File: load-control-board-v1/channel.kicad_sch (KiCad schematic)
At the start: 34 parts, among them Q1 AO3400A, Q2 AO3400A, Q3 IRFP7530PBF, U10 OPA188xxDBV, U11 OPA188xxDBV, U12 INA186A1IDCKR

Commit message: Move to layout stage
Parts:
- TP0a1, TP0c1, TP2, TP3: footprint TestPoint:TestPoint_Keystone_5019_Miniature -> TestPoint:TestPoint_Keystone_5015_Micro_Mini
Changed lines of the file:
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@@
 			)
 		)
-		(property "Footprint" "TestPoint:TestPoint_Keystone_5019_Miniature"
+		(property "Footprint" "TestPoint:TestPoint_Keystone_5015_Micro_Mini"
 			(at 190.5 38.1 0)
 			(effects
@@
 			)
 		)
-		(property "Footprint" "TestPoint:TestPoint_Keystone_5019_Miniature"
+		(property "Footprint" "TestPoint:TestPoint_Keystone_5015_Micro_Mini"
 			(at 77.47 60.96 0)
 			(effects
@@
 			)
 		)
-		(property "Footprint" "TestPoint:TestPoint_Keystone_5019_Miniature"
+		(property "Footprint" "TestPoint:TestPoint_Keystone_5015_Micro_Mini"
 			(at 115.57 43.18 0)
 			(effects
@@
 			)
 		)
-		(property "Footprint" "TestPoint:TestPoint_Keystone_5019_Miniature"
+		(property "Footprint" "TestPoint:TestPoint_Keystone_5015_Micro_Mini"
 			(at 204.47 133.35 0)
 			(effects

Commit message: initial layout
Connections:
- net at R21.1, R22.2, R23.2: no longer C15.1, R20.1
- net at R21.2, TP2.1, U10.1: now also C15.1, R20.1
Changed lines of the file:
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@@
+	)
+	(junction
+		(at 86.36 72.39)
+		(diameter 0)
+		(color 0 0 0 0)
 	)
 	(junction
@@
 	)
 	(junction
-		(at 86.36 72.39)
-		(diameter 0)
-		(color 0 0 0 0)
-	)
-	(junction
 		(at 91.44 60.96)
 		(diameter 0)
@@
 		(color 0 0 0 0)
 	)
-	(junction
-		(at 86.36 60.96)
-		(diameter 0)
-		(color 0 0 0 0)
-	)
 	(wire
 		(pts
@@
 	(wire
 		(pts
+			(xy 86.36 67.31) (xy 72.39 67.31)
+		)
+		(stroke
+			(width 0)
+			(type default)
+		)
+	)
+	(wire
+		(pts
+			(xy 72.39 67.31) (xy 72.39 60.96)
+		)
+		(stroke
+			(width 0)
+			(type default)
+		)
+	)
+	(wire
+		(pts
 			(xy 185.42 45.72) (xy 200.66 45.72)
 		)
@@
 	(wire
 		(pts
-			(xy 86.36 60.96) (xy 91.44 60.96)
+			(xy 81.28 60.96) (xy 91.44 60.96)
 		)
 		(stroke
@@
 	(wire
 		(pts
-			(xy 81.28 60.96) (xy 86.36 60.96)
-		)
-		(stroke
-			(width 0)
-			(type default)
-		)
-	)
-	(wire
-		(pts
 			(xy 106.68 60.96) (xy 106.68 69.85)
 		)
@@
 	(wire
 		(pts
+			(xy 86.36 72.39) (xy 86.36 67.31)
+		)
+		(stroke
+			(width 0)
+			(type default)
+		)
+	)
+	(wire
+		(pts
 			(xy 182.88 45.72) (xy 185.42 45.72)
 		)
@@
 		)
 		(stroke
-			(width 0)
-			(type default)
-		)
-	)
-	(wire
-		(pts
-			(xy 86.36 60.96) (xy 86.36 72.39)
-		)
-		(stroke

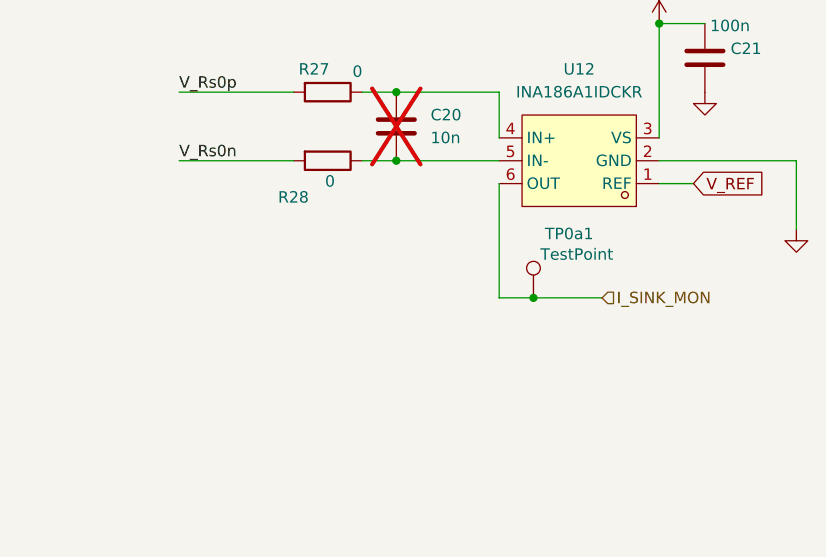
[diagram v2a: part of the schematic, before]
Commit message: Define the connector pinout to control board, import current connector
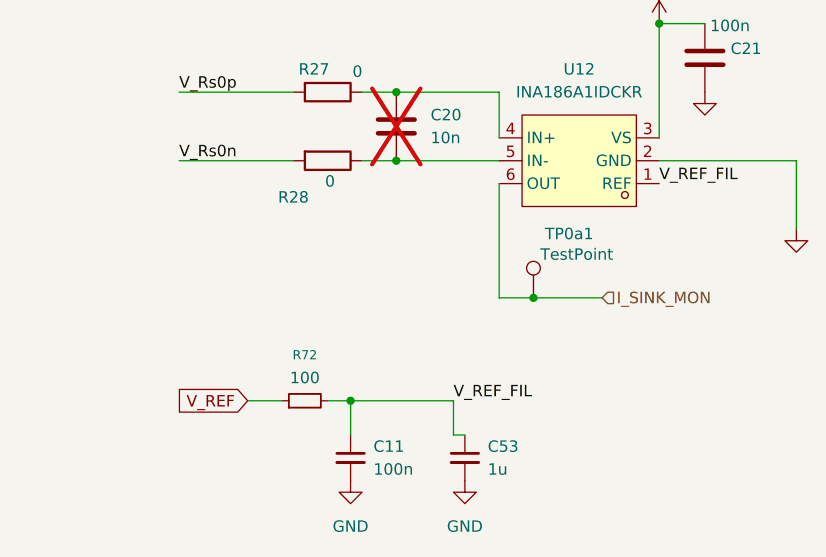
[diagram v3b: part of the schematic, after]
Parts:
- added C11: 100n, symbol Device:C_Small
- added C53: 1u, symbol Device:C_Small
- added R72: 100, symbol Device:R_Small
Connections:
- net GND: now also C11.2, C53.2
- net V_REF: now also R72.1; no longer U12.1 (REF)
- new net V_REF_FIL: C11.1, C53.1, R72.2, U12.1 (REF)

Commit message: layout before check
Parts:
- C11: footprint (none) -> Capacitor_SMD:C_0603_1608Metric
- C53, R72: footprint (none) -> Resistor_SMD:R_0603_1608Metric
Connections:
- net 5V renamed +5V
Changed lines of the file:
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@@
 			)
 		)
-		(property "Value" "5V"
+		(property "Value" "+5V"
 			(at 213.614 98.806 0)
 			(effects
@@
 			)
 		)
-		(property "Footprint" ""
+		(property "Footprint" "Capacitor_SMD:C_0603_1608Metric"
 			(at 179.07 151.13 0)
 			(effects
@@
 			)
 		)
-		(property "Footprint" ""
+		(property "Footprint" "Resistor_SMD:R_0603_1608Metric"
 			(at 191.77 151.13 0)
 			(effects
@@
 			)
 		)
-		(property "Footprint" ""
+		(property "Footprint" "Resistor_SMD:R_0603_1608Metric"
 			(at 173.99 144.78 0)
 			(effects

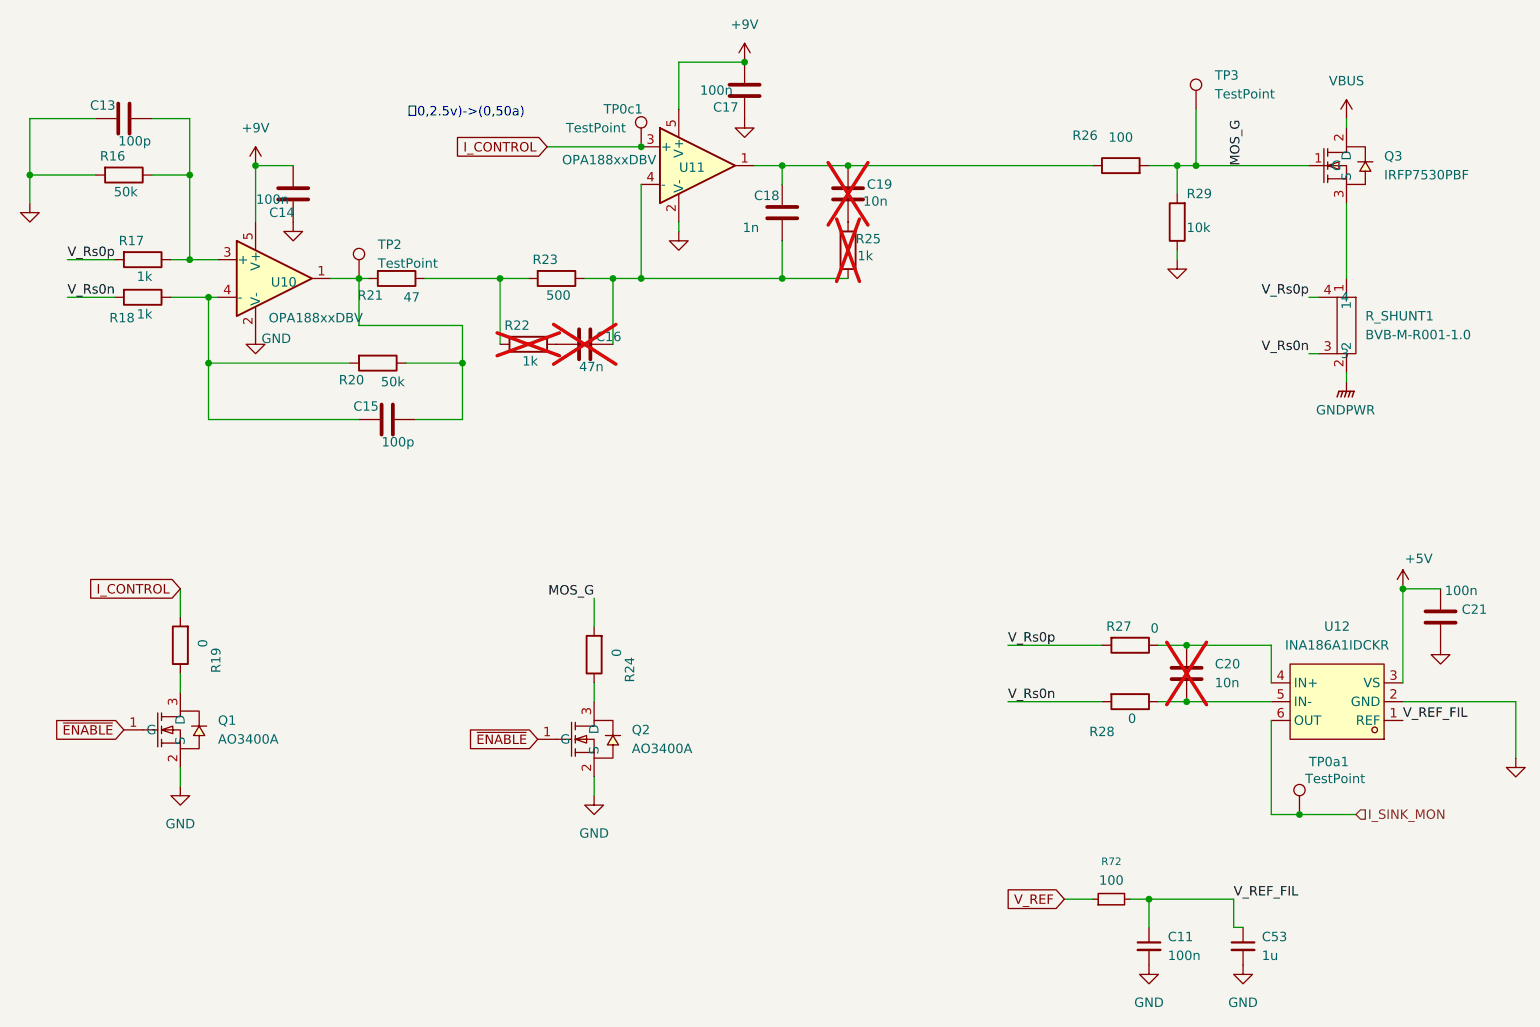
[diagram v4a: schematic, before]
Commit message: Add filled zone for mosfet, change terminal to from THO to SMT
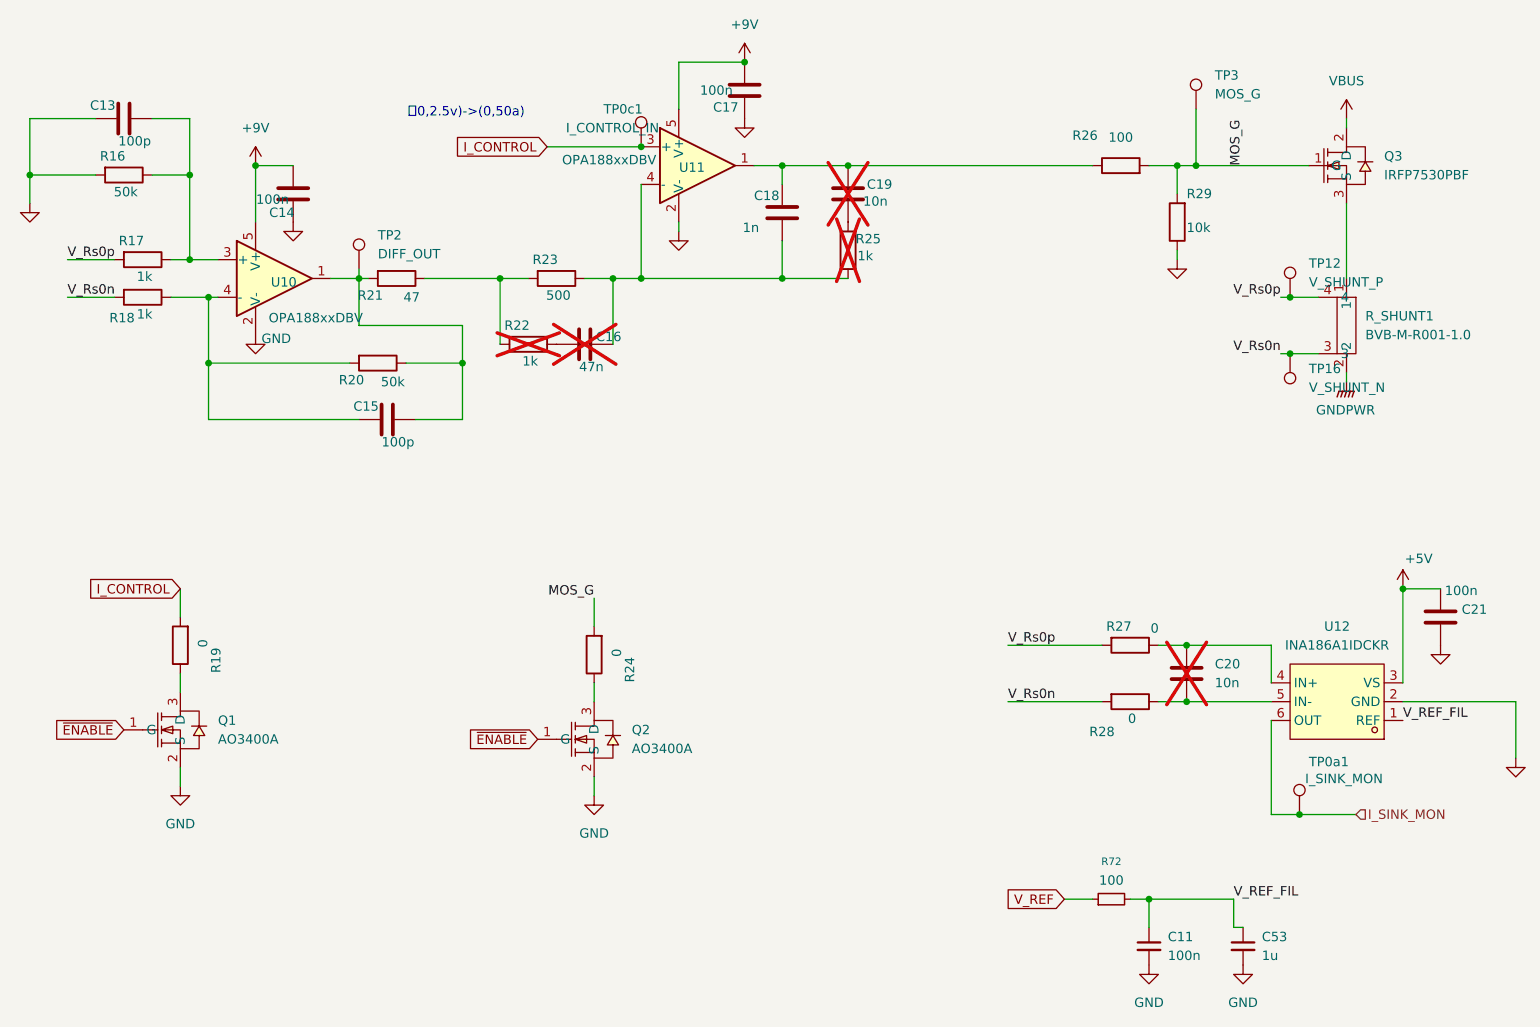
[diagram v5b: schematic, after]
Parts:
- added TP12: V_SHUNT_P, programmable-load-library:SMD_RH-5015, symbol Connector:TestPoint
- added TP16: V_SHUNT_N, programmable-load-library:SMD_RH-5015, symbol Connector:TestPoint
- Q3: footprint programmable-load-library:PG-TO247-3_L15.9-W5.2-P5.44-L -> programmable-load-library:PG-TO247-3_L15.9-W5.2-P5.44-L_1_Horizontal
- TP0a1: value TestPoint -> I_SINK_MON; footprint TestPoint:TestPoint_Keystone_5015_Micro_Mini -> programmable-load-library:SMD_RH-5015
- TP0c1: value TestPoint -> I_CONTROL_IN; footprint TestPoint:TestPoint_Keystone_5015_Micro_Mini -> programmable-load-library:SMD_RH-5015
- TP2: value TestPoint -> DIFF_OUT; footprint TestPoint:TestPoint_Keystone_5015_Micro_Mini -> programmable-load-library:SMD_RH-5015
- TP3: value TestPoint -> MOS_G; footprint TestPoint:TestPoint_Keystone_5015_Micro_Mini -> programmable-load-library:SMD_RH-5015
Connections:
- net V_Rs0n: now also TP16.1
- net V_Rs0p: now also TP12.1
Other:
- moved on the sheet: TP2
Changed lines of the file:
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@@
 	)
 	(junction
+		(at 198.12 71.12)
+		(diameter 0)
+		(color 0 0 0 0)
+	)
+	(junction
 		(at 182.88 45.72)
 		(diameter 0)
@@
 	)
 	(junction
+		(at 198.12 63.5)
+		(diameter 0)
+		(color 0 0 0 0)
+	)
+	(junction
 		(at 52.07 63.5)
 		(diameter 0)
@@
 	(wire
 		(pts
-			(xy 200.66 71.12) (xy 201.93 71.12)
+			(xy 196.85 71.12) (xy 198.12 71.12)
 		)
 		(stroke
@@
 	(wire
 		(pts
+			(xy 198.12 63.5) (xy 201.93 63.5)
+		)
+		(stroke
+			(width 0)
+			(type default)
+		)
+	)
+	(wire
+		(pts
 			(xy 33.02 58.42) (xy 39.37 58.42)
 		)
@@
 	(wire
 		(pts
+			(xy 198.12 71.12) (xy 201.93 71.12)
+		)
+		(stroke
+			(width 0)
+			(type default)
+		)
+	)
+	(wire
+		(pts
 			(xy 27.94 46.99) (xy 27.94 50.8)
 		)
@@
 	(wire
 		(pts
-			(xy 200.66 63.5) (xy 201.93 63.5)
+			(xy 196.85 63.5) (xy 198.12 63.5)
 		)
 		(stroke
@@
 	(wire
 		(pts
+			(xy 72.39 59.69) (xy 72.39 60.96)
+		)
+		(stroke
+			(width 0)
+			(type default)
+		)
+	)
+	(wire
+		(pts
 			(xy 68.58 60.96) (xy 72.39 60.96)
 		)
@@
 	)
 	(label "V_Rs0n"
-		(at 200.66 71.12 180)
+		(at 196.85 71.12 180)
 		(effects
 			(font
@@
 	)
 	(label "V_Rs0p"
-		(at 200.66 63.5 180)
+		(at 196.85 63.5 180)
 		(effects
 			(font
@@
 			)
 		)
-		(property "Value" "TestPoint"
+		(property "Value" "MOS_G"
 			(at 187.96 36.0679 0)
 			(effects
@@
 			)
 		)
-		(property "Footprint" "TestPoint:TestPoint_Keystone_5015_Micro_Mini"
+		(property "Footprint" "programmable-load-library:SMD_RH-5015"
 			(at 190.5 38.1 0)
 			(effects
@@
 	(symbol
 		(lib_id "Connector:TestPoint")
-		(at 72.39 60.96 0)
+		(at 72.39 59.69 0)
 		(unit 1)
 		(exclude_from_sim no)
@@
 		(fields_autoplaced yes)
 		(property "Reference" "TP2"
-			(at 74.93 56.3879 0)
+			(at 74.93 55.1179 0)
 			(effects
 				(font
@@
 			)
 		)
-		(property "Value" "TestPoint"
-			(at 74.93 58.9279 0)
+		(property "Value" "DIFF_OUT"
+			(at 74.93 57.6579 0)
 			(effects
 				(font
@@
 			)
 		)
-		(property "Footprint" "TestPoint:TestPoint_Keystone_5015_Micro_Mini"
-			(at 77.47 60.96 0)
+		(property "Footprint" "programmable-load-library:SMD_RH-5015"
+			(at 77.47 59.69 0)
 			(effects
 				(font
@@
 		)
 		(property "Datasheet" "~"
-			(at 77.47 60.96 0)
+			(at 77.47 59.69 0)
 			(effects
 				(font
@@
 		)
 		(property "Description" "test point"
-			(at 72.39 60.96 0)
+			(at 72.39 59.69 0)
 			(effects
 				(font
@@
 			)
 		)
-		(property "Value" "TestPoint"
+		(property "Value" "I_CONTROL_IN"
 			(at 100.33 40.64 0)
 			(effects
@@
 			)
 		)
-		(property "Footprint" "TestPoint:TestPoint_Keystone_5015_Micro_Mini"
+		(property "Footprint" "programmable-load-library:SMD_RH-5015"
 			(at 115.57 43.18 0)
 			(effects
@@
 	)
 	(symbol
+		(lib_id "Connector:TestPoint")
+		(at 198.12 63.5 0)
+		(unit 1)
+		(exclude_from_sim no)
+		(in_bom yes)
+		(on_board yes)
+		(dnp no)
+		(fields_autoplaced yes)
+		(property "Reference" "TP12"
+			(at 200.66 58.9279 0)
+			(effects
+				(font
+					(size 1.27 1.27)
+				)
+				(justify left)
+			)
+		)
+		(property "Value" "V_SHUNT_P"
+			(at 200.66 61.4679 0)
+			(effects
+				(font
+					(size 1.27 1.27)
+				)
+				(justify left)
+			)
+		)
+		(property "Footprint" "programmable-load-library:SMD_RH-5015"
+			(at 203.2 63.5 0)
+			(effects
+				(font
+					(size 1.27 1.27)
+				)
+				(hide yes)
+			)
+		)
+		(property "Datasheet" "~"
+			(at 203.2 63.5 0)
+			(effects
+				(font
+					(size 1.27 1.27)
+				)
+				(hide yes)
+			)
+		)
+		(property "Description" "test point"
+			(at 198.12 63.5 0)
+			(effects
+				(font
+					(size 1.27 1.27)
+				)
+				(hide yes)
+			)
+		)
+		(pin "1"
+		)
+		(instances
+			(project "load-control-board-v1"
+				(path "/932aba27-7b64-4a5e-ae3c-58efe17592af/13334eb8-ba95-4a2f-940f-a682d806f744"
+					(reference "TP13")
+					(unit 1)
+				)
+				(path "/932aba27-7b64-4a5e-ae3c-58efe17592af/6bc47c43-2a61-4add-a64d-33ab3822194a"
+					(reference "TP14")
+					(unit 1)
+				)
+				(path "/932aba27-7b64-4a5e-ae3c-58efe17592af/705a8778-6422-475b-b5ab-00ba27249c43"
+					(reference "TP15")
+					(unit 1)
+				)
+				(path "/932aba27-7b64-4a5e-ae3c-58efe17592af/d175793d-7a2d-40c2-8abf-93894290eb6d"
+					(reference "TP12")
+					(unit 1)
+				)
+			)
+		)
+	)
+	(symbol
 		(lib_id "power:GND")
 		(at 182.88 58.42 0)
@@
 	)
 	(symbol
+		(lib_id "Connector:TestPoint")
+		(at 198.12 71.12 180)
+		(unit 1)
+		(exclude_from_sim no)
+		(in_bom yes)
+		(on_board yes)
+		(dnp no)
+		(fields_autoplaced yes)
+		(property "Reference" "TP16"
+			(at 200.66 73.1519 0)
+			(effects
+				(font
+					(size 1.27 1.27)
+				)
+				(justify right)
+			)
+		)
+		(property "Value" "V_SHUNT_N"
+			(at 200.66 75.6919 0)
+			(effects
+				(font
+					(size 1.27 1.27)
+				)
+				(justify right)
+			)
+		)
+		(property "Footprint" "programmable-load-library:SMD_RH-5015"
+			(at 193.04 71.12 0)
+			(effects
+				(font
+					(size 1.27 1.27)
+				)
+				(hide yes)
+			)
+		)
+		(property "Datasheet" "~"
+			(at 193.04 71.12 0)
+			(effects
+				(font
+					(size 1.27 1.27)
+				)
+				(hide yes)
+			)
+		)
+		(property "Description" "test point"
+			(at 198.12 71.12 0)
+			(effects
+				(font
+					(size 1.27 1.27)
+				)
+				(hide yes)
+			)
+		)
+		(pin "1"
+		)
+		(instances
+			(project "load-control-board-v1"
+				(path "/932aba27-7b64-4a5e-ae3c-58efe17592af/13334eb8-ba95-4a2f-940f-a682d806f744"
+					(reference "TP17")
+					(unit 1)
+				)
+				(path "/932aba27-7b64-4a5e-ae3c-58efe17592af/6bc47c43-2a61-4add-a64d-33ab3822194a"
+					(reference "TP18")
+					(unit 1)
+				)
+				(path "/932aba27-7b64-4a5e-ae3c-58efe17592af/705a8778-6422-475b-b5ab-00ba27249c43"
+					(reference "TP19")
+					(unit 1)
+				)
+				(path "/932aba27-7b64-4a5e-ae3c-58efe17592af/d175793d-7a2d-40c2-8abf-93894290eb6d"
+					(reference "TP16")
+					(unit 1)
+				)
+			)
+		)
+	)
+	(symbol
 		(lib_id "programmable-load-library:IRFP7530PBF")
 		(at 205.74 45.72 0)
@@
 			)
 		)
-		(property "Footprint" "programmable-load-library:PG-TO247-3_L15.9-W5.2-P5.44-L"
+		(property "Footprint" "programmable-load-library:PG-TO247-3_L15.9-W5.2-P5.44-L_1_Horizontal"
 			(at 205.74 58.42 0)
 			(effects
@@
 			)
 		)
-		(property "Value" "TestPoint"
+		(property "Value" "I_SINK_MON"
 			(at 200.152 128.524 0)
 			(effects
@@
 			)
 		)
-		(property "Footprint" "TestPoint:TestPoint_Keystone_5015_Micro_Mini"
+		(property "Footprint" "programmable-load-library:SMD_RH-5015"
 			(at 204.47 133.35 0)
 			(effects

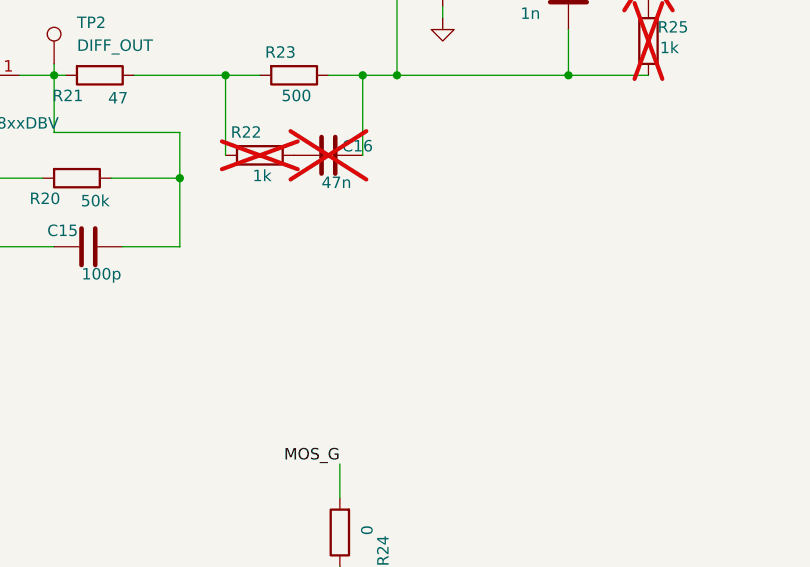
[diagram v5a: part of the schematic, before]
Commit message: Complete second times layout (no copper filled)
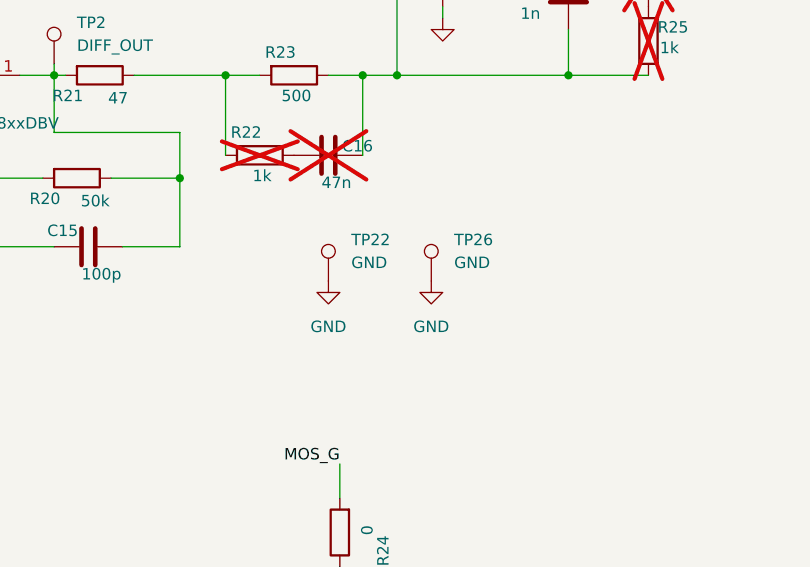
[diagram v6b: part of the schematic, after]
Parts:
- added TP22, TP26: GND, programmable-load-library:SMD_RH-5015, symbol Connector:TestPoint
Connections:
- net GND: now also TP22.1, TP26.1
